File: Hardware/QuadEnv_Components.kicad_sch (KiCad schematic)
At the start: 50 parts, among them J1 Eurorack_10_pin_power, J2 Conn_01x04_Male, J3 Conn_01x04_Male, J4 Conn_01x04_Male, J5 Conn_01x04_Male, U1 STM32C031C6T, U2 LD1117-3.3-4Tab, U3 TL074

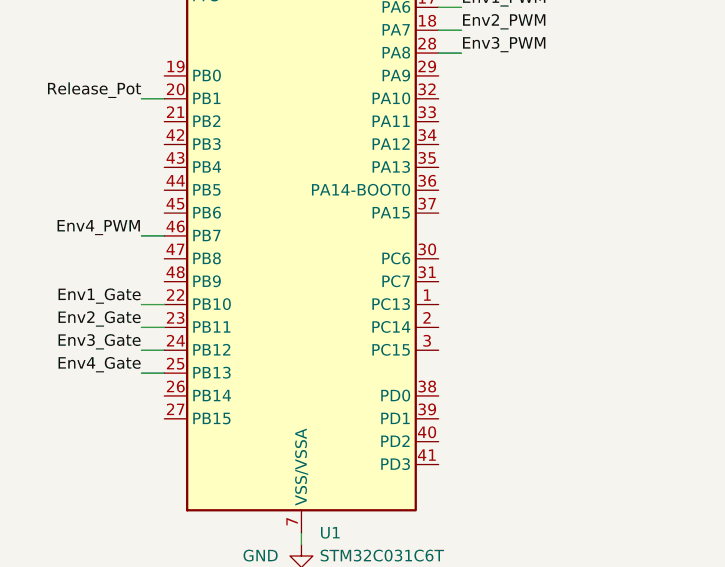
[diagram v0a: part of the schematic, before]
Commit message: Started adding UART
Though tests show that UART1 is not connected by default on Nucleo
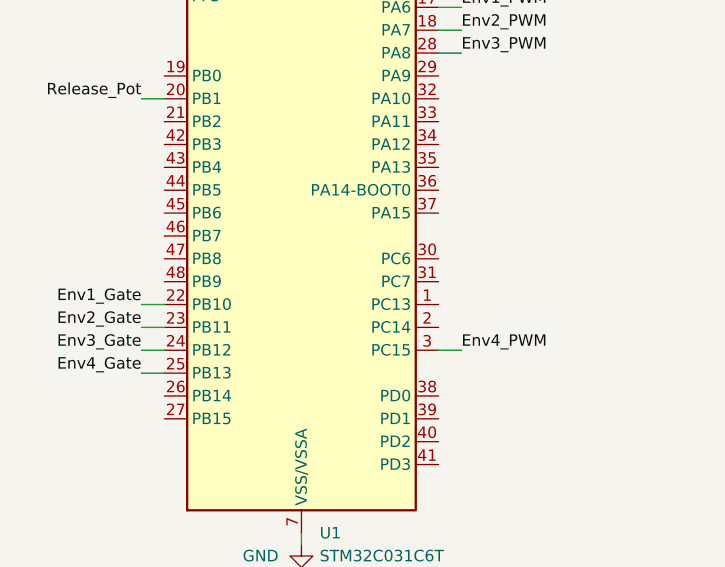
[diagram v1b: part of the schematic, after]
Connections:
- net Env4_PWM: now also U1.3 (PC15); no longer U1.46 (PB7)
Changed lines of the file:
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@@
     (stroke (width 0) (type default) (color 0 0 0 0))
   )
-  (wire (pts (xy 38.1 85.09) (xy 35.56 85.09))
+  (wire (pts (xy 68.58 97.79) (xy 71.12 97.79))
     (stroke (width 0) (type default) (color 0 0 0 0))
   )
@@
     (effects (font (size 1.27 1.27)) (justify left bottom))
   )
-  (label "Env4_PWM" (at 35.56 85.09 180)
-    (effects (font (size 1.27 1.27)) (justify right bottom))
+  (label "Env4_PWM" (at 71.12 97.79 0)
+    (effects (font (size 1.27 1.27)) (justify left bottom))
   )
   (label "Env1_LED" (at 184.15 130.81 0)
